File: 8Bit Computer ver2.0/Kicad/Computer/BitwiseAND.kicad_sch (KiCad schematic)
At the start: 5 parts, among them IC30 SN74LVC1G14DBVR, IC36 SN74HCS74DR, IC37 SN74HCS574DGSR, IC5 SN74HCS08DR, IC9 SN74HCS08DR

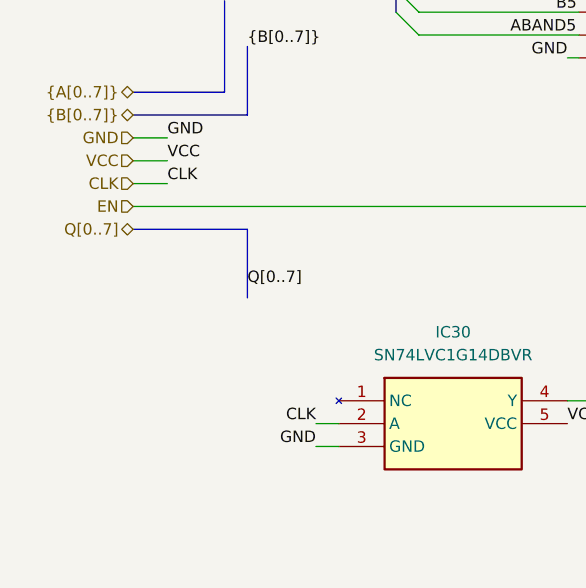
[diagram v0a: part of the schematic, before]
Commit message: Kicad,parts
Kicad:
added FlagRegister
began Inc, Comp
parts:
added comparator for P>Q 682
added faster sram 12ns AS7C
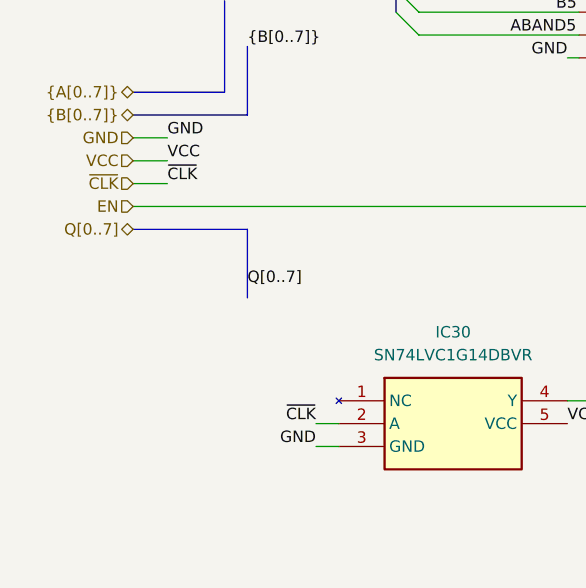
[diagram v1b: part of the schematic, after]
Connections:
- net CLK renamed ~{CLK}
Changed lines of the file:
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@@
 		)
 	)
-	(label "CLK"
+	(label "~{CLK}"
 		(at 69.85 128.27 180)
 		(effects
@@
 		)
 	)
-	(label "CLK"
+	(label "~{CLK}"
 		(at 53.34 101.6 0)
 		(effects
@@
 		)
 	)
-	(hierarchical_label "CLK"
+	(hierarchical_label "~{CLK}"
 		(shape input)
 		(at 49.53 101.6 180)

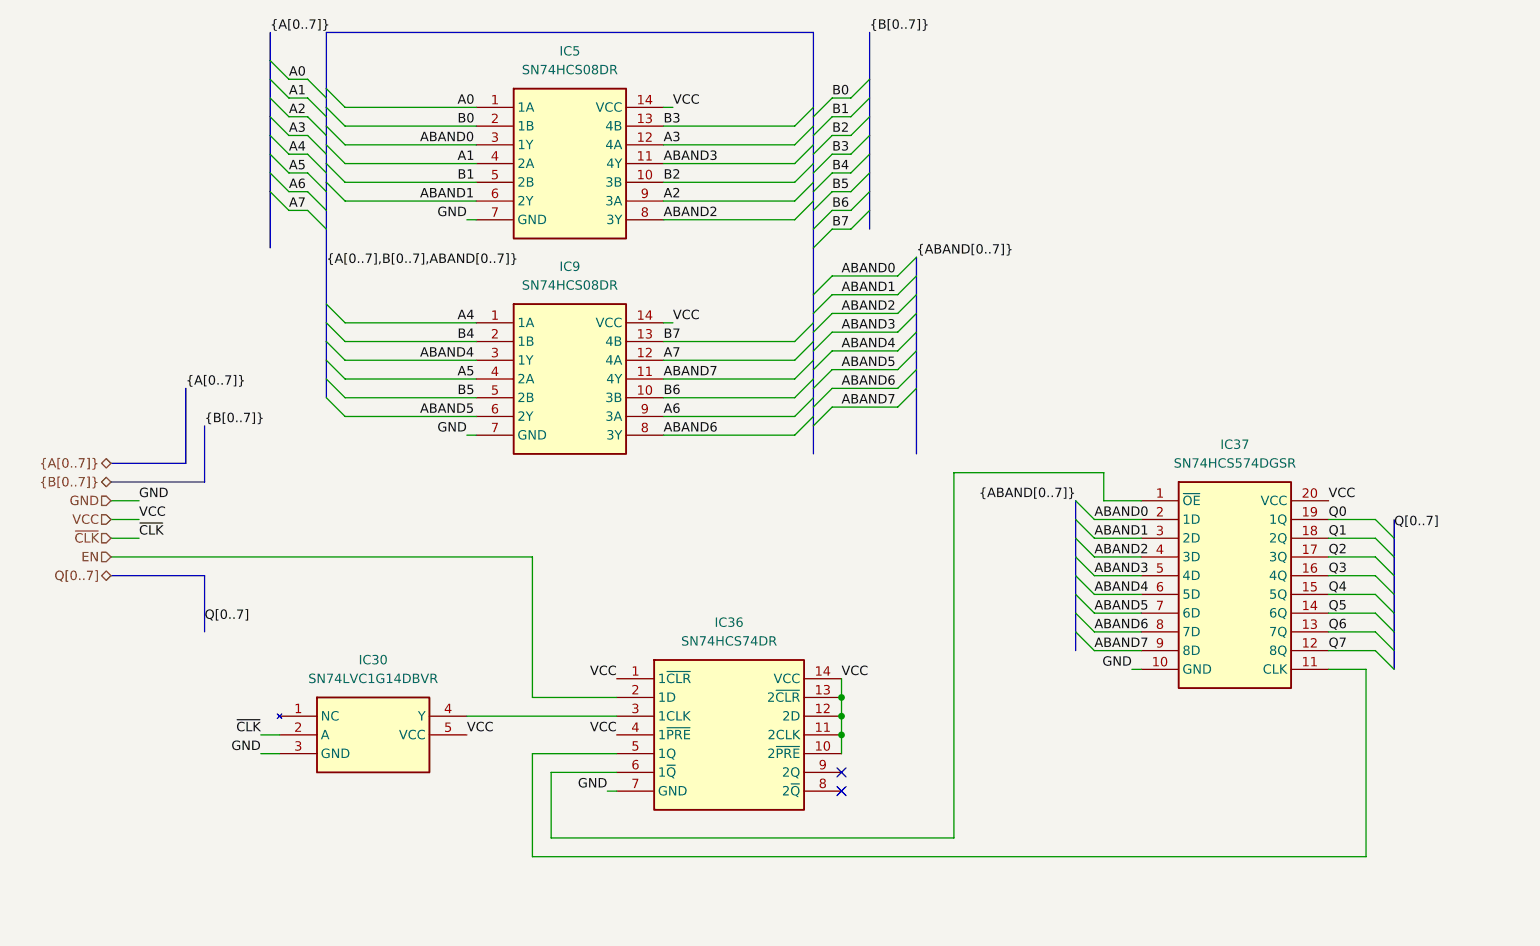
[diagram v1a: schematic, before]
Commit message: parts,Kicad
parts:
changed 8xDlatch HCS to ABT 574
waiting for SRAM CAD Model
Kicad:
imported AHC types of ICs
added ProgrammeCounter
finished Comparator
changed all HCS to AHC except 3in OR ->no AHC Version
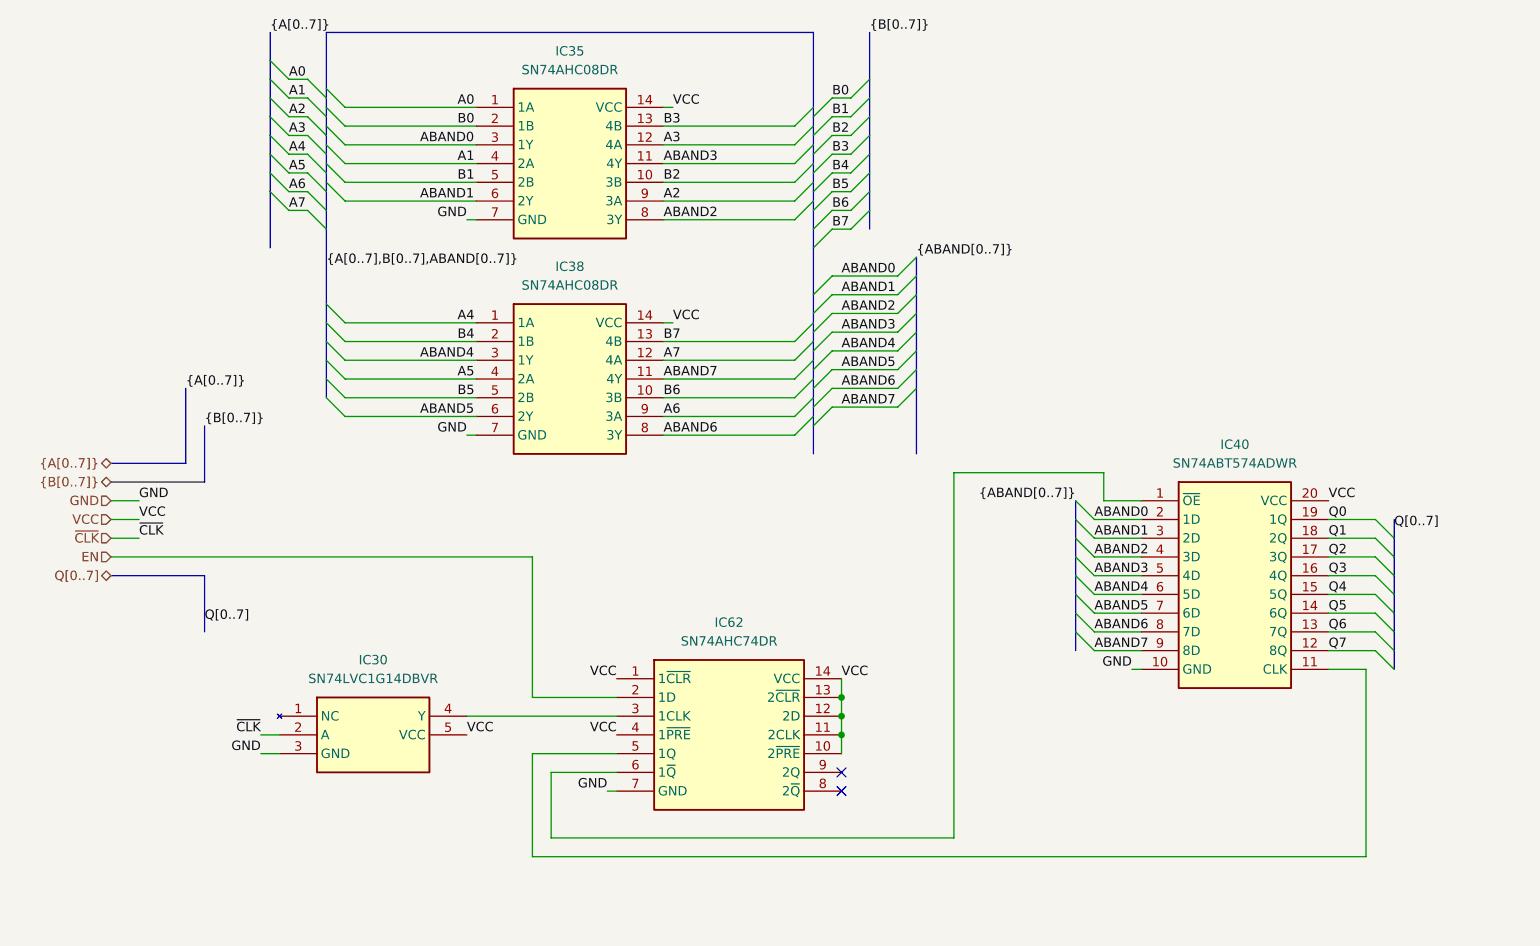
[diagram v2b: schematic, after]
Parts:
- removed IC36: SN74HCS74DR, Samacsys:SOIC127P600X175-14N, symbol Samacsys:SN74HCS74DR
- removed IC37: SN74HCS574DGSR, Samacsys:SOP50P490X110-20N, symbol Samacsys:SN74HCS574DGSR
- removed IC5, IC9: SN74HCS08DR, Samacsys:SOIC127P600X175-14N, symbol Samacsys:SN74HCS08DR
- added IC35, IC38: SN74AHC08DR, Samacsys:SOIC127P600X175-14N, symbol Samacsys:SN74AHC08DR
- added IC40: SN74ABT574ADWR, Samacsys:SOIC127P1030X265-20N, symbol Samacsys:SN74ABT574ADWR
- added IC62: SN74AHC74DR, Samacsys:SOIC127P600X175-14N, symbol Samacsys:SN74AHC74DR
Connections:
- net A0: now also IC35.1 (1A)
- net A1: now also IC35.4 (2A)
- net A2: now also IC35.9 (3A)
- net A3: now also IC35.12 (4A)
- net A4: now also IC38.1 (1A)
- net A5: now also IC38.4 (2A)
- net A6: now also IC38.9 (3A)
- net A7: now also IC38.12 (4A)
- net ABAND0: now also IC35.3 (1Y), IC40.2 (1D)
- net ABAND1: now also IC35.6 (2Y), IC40.3 (2D)
- net ABAND2: now also IC35.8 (3Y), IC40.4 (3D)
- net ABAND3: now also IC35.11 (4Y), IC40.5 (4D)
- net ABAND4: now also IC38.3 (1Y), IC40.6 (5D)
- net ABAND5: now also IC38.6 (2Y), IC40.7 (6D)
- net ABAND6: now also IC38.8 (3Y), IC40.8 (7D)
- net ABAND7: now also IC38.11 (4Y), IC40.9 (8D)
- net B0: now also IC35.2 (1B)
- net B1: now also IC35.5 (2B)
- net B2: now also IC35.10 (3B)
- net B3: now also IC35.13 (4B)
- net B4: now also IC38.2 (1B)
- net B5: now also IC38.5 (2B)
- net B6: now also IC38.10 (3B)
- net B7: now also IC38.13 (4B)
- net EN: now also IC62.2 (1D)
- net GND: now also IC35.7 (GND), IC38.7 (GND), IC40.10 (GND), IC62.7 (GND)
- net Q0: now also IC40.19 (1Q)
- net Q1: now also IC40.18 (2Q)
- net Q2: now also IC40.17 (3Q)
- net Q3: now also IC40.16 (4Q)
- net Q4: now also IC40.15 (5Q)
- net Q5: now also IC40.14 (6Q)
- net Q6: now also IC40.13 (7Q)
- net Q7: now also IC40.12 (8Q)
- net VCC: now also IC35.14 (VCC), IC38.14 (VCC), IC40.20 (VCC), IC62.1 (1~{CLR}), IC62.10 (2~{PRE}), IC62.11 (2CLK), IC62.12 (2D), IC62.13 (2~{CLR}), IC62.14 (VCC), IC62.4 (1~{PRE})
- net at IC30.4 (Y): now also IC62.3 (1CLK)
- new net: IC40.11 (CLK), IC62.5 (1Q)
- new net: IC40.1 (~{OE}), IC62.6 (1~{Q})

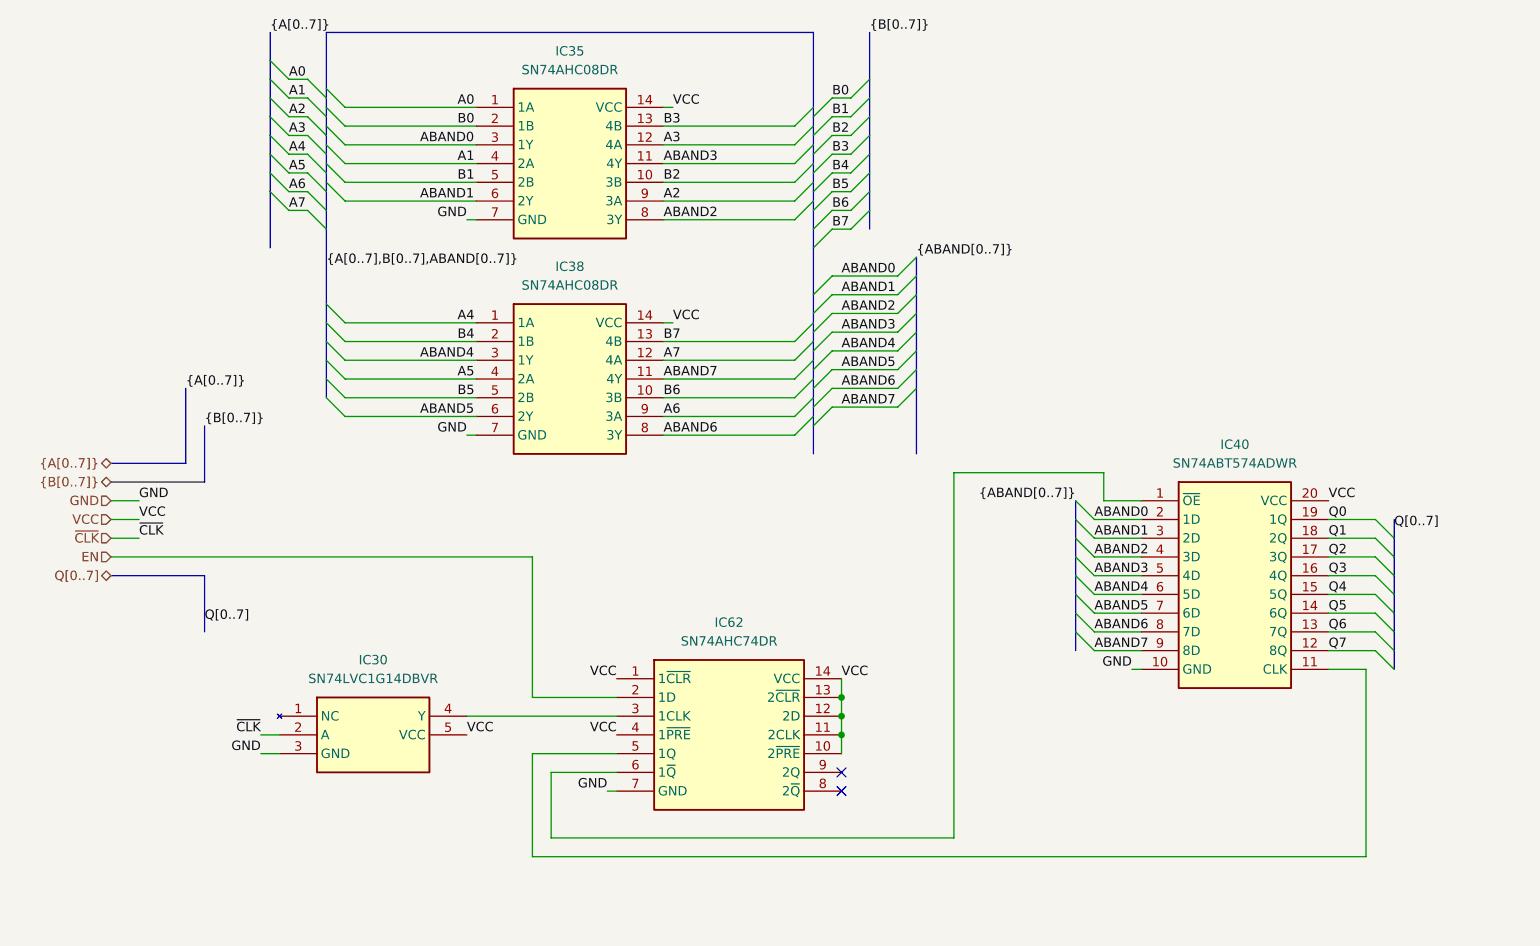
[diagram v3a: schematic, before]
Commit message: Kicad, parts
Parts:
added Leds
Kicad:
added Input Output
changed Q bus to DAT bus
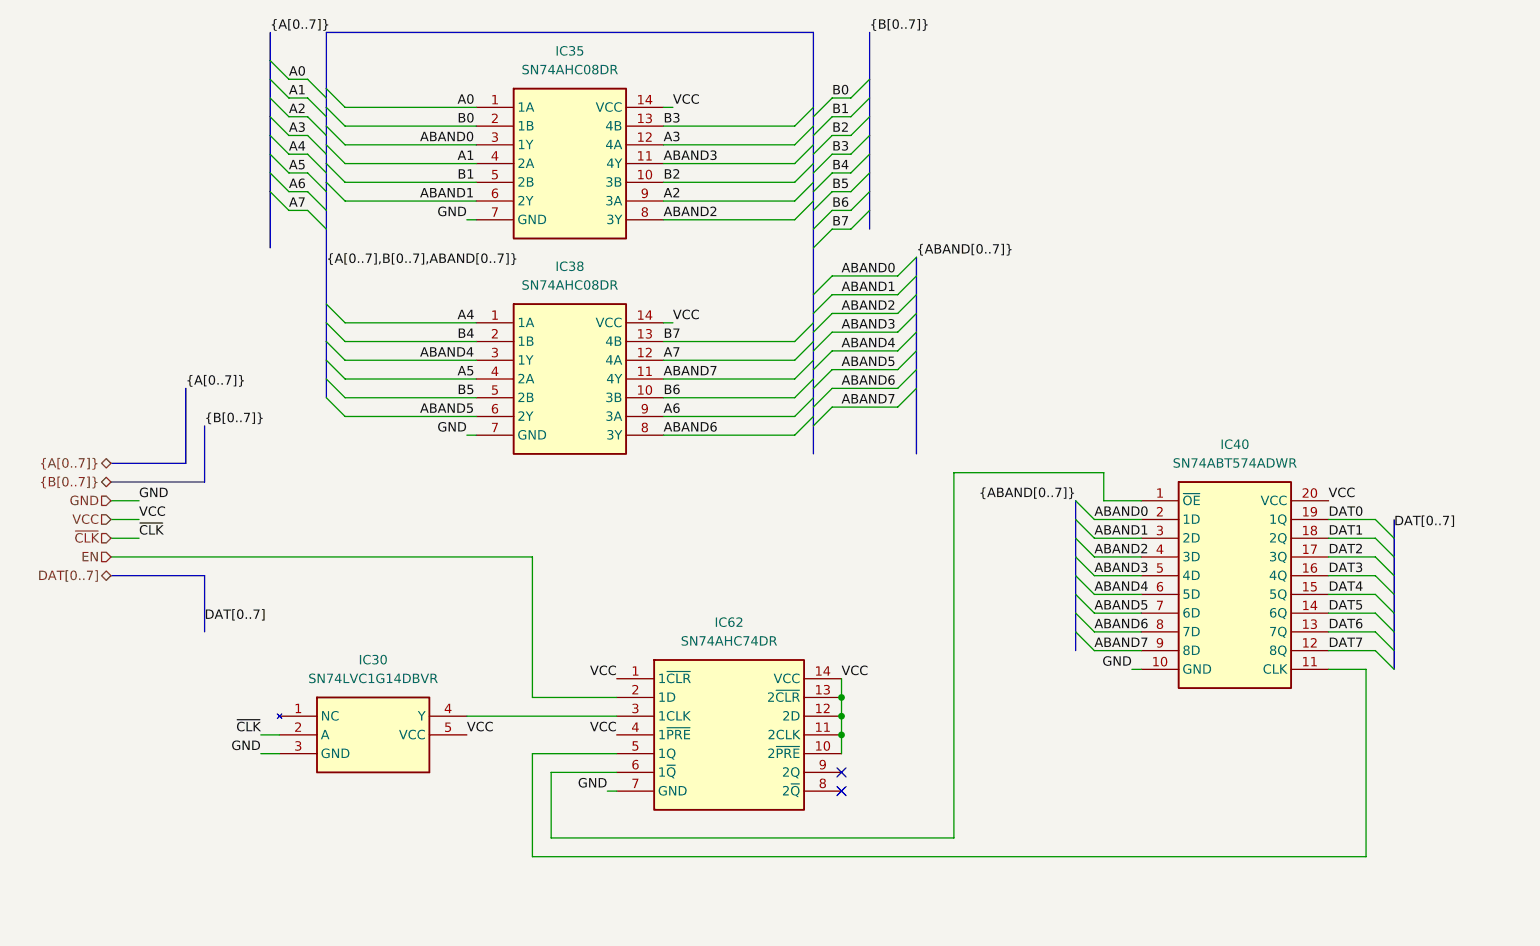
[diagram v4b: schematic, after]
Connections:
- net Q0 renamed DAT0
- net Q1 renamed DAT1
- net Q2 renamed DAT2
- net Q3 renamed DAT3
- net Q4 renamed DAT4
- net Q5 renamed DAT5
- net Q6 renamed DAT6
- net Q7 renamed DAT7
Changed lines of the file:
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@@
 		)
 	)
-	(label "Q0"
+	(label "DAT0"
 		(at 214.63 99.06 0)
 		(effects
@@
 		)
 	)
-	(label "Q7"
+	(label "DAT7"
 		(at 214.63 116.84 0)
 		(effects
@@
 		)
 	)
-	(label "Q4"
+	(label "DAT4"
 		(at 214.63 109.22 0)
 		(effects
@@
 		)
 	)
-	(label "Q3"
+	(label "DAT3"
 		(at 214.63 106.68 0)
 		(effects
@@
 		)
 	)
-	(label "Q1"
+	(label "DAT1"
 		(at 214.63 101.6 0)
 		(effects
@@
 		)
 	)
-	(label "Q2"
+	(label "DAT2"
 		(at 214.63 104.14 0)
 		(effects
@@
 		)
 	)
-	(label "Q5"
+	(label "DAT5"
 		(at 214.63 111.76 0)
 		(effects
@@
 		)
 	)
-	(label "Q[0..7]"
+	(label "DAT[0..7]"
 		(at 62.23 113.03 0)
 		(effects
@@
 		)
 	)
-	(label "Q6"
+	(label "DAT6"
 		(at 214.63 114.3 0)
 		(effects
@@
 		)
 	)
-	(label "Q[0..7]"
+	(label "DAT[0..7]"
 		(at 223.52 100.33 0)
 		(effects
@@
 		)
 	)
-	(hierarchical_label "Q[0..7]"
+	(hierarchical_label "DAT[0..7]"
 		(shape tri_state)
 		(at 49.53 106.68 180)

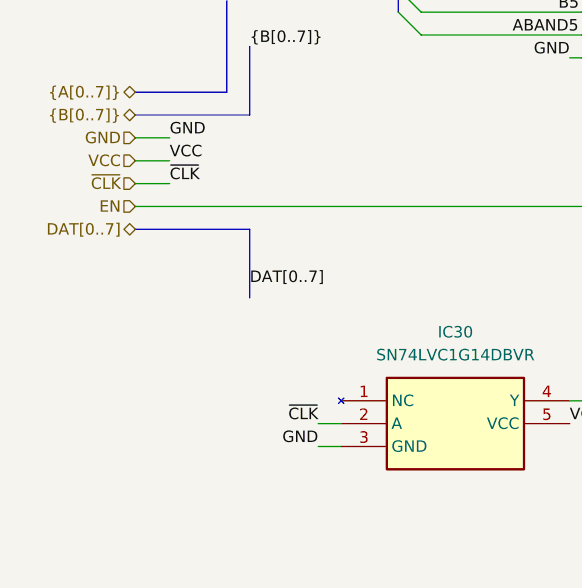
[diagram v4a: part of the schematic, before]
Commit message: Kicad, parts
parts:
added USB C PD Triggerboard
added Delay Chip for 90ns
added Push Button
Kicad:
added USB C PD Triggerboard
added rising edge detector via Delay and Xor for Accept Push Button
added VBUS net
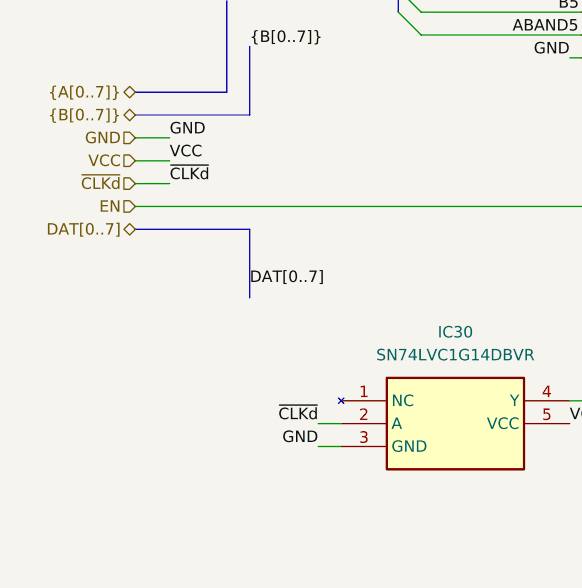
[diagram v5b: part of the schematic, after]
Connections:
- net ~{CLK} renamed ~{CLKd}
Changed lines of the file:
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@@
 		)
 	)
-	(label "~{CLK}"
+	(label "~{CLKd}"
 		(at 69.85 128.27 180)
 		(effects
@@
 		)
 	)
-	(label "~{CLK}"
+	(label "~{CLKd}"
 		(at 53.34 101.6 0)
 		(effects
@@
 		)
 	)
-	(hierarchical_label "~{CLK}"
+	(hierarchical_label "~{CLKd}"
 		(shape input)
 		(at 49.53 101.6 180)
